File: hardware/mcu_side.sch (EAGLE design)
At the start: 31 parts, among them CON1 JST-ZR-06, Q1 BSS138LT3G, U1 STM32F031G6U6

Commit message: Add start module
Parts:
- added SM_3.3V, SM_GND, SM_KILL, SM_START: PAD-SMD-ROUND-1.27PAD, Isaks Bibliotek:PAD-SMD-ROUND-1.27PAD
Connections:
- new net KILL: SM_KILL.1, U1.PA3
- new net START: SM_START.1, U1.PA2
- net 3.3V: now also SM_3.3V.1
- net GND: now also SM_GND.1
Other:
- note added: "Check before production: - Check Hardware app note - 3.3V reg again. - That the FB on servo indeed is a pot and does not need V_divider - Double check pinout - Double check ERC + DRC - Check Silcscreen"
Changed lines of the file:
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@@
 <drawing>
 <settings>
-<setting alwaysvectorfont="no"/>
+<setting alwaysvectorfont="yes"/>
 <setting verticaltext="up"/>
 </settings>
@@
 <schematic_group name="I2C_PULLUP"/>
 <schematic_group name="STEERING_SERVO_FEEDBACK"/>
+<schematic_group name="START_MODULE"/>
 </groups>
 <parts>
@@
 <part name="SUPPLY13" library="Isaks Bibliotek" library_urn="urn:adsk.eagle:library:11889733" deviceset="3.3V" device=""/>
 <part name="GND14" library="Isaks Bibliotek" library_urn="urn:adsk.eagle:library:11889733" deviceset="GND" device=""/>
+<part name="SM_3.3V" library="Isaks Bibliotek" library_urn="urn:adsk.eagle:library:11889733" deviceset="PAD-SMD-ROUND-1.27" device="PAD" package3d_urn="urn:adsk.eagle:package:13270955/1"/>
+<part name="SM_START" library="Isaks Bibliotek" library_urn="urn:adsk.eagle:library:11889733" deviceset="PAD-SMD-ROUND-1.27" device="PAD" package3d_urn="urn:adsk.eagle:package:13270955/1"/>
+<part name="SUPPLY14" library="Isaks Bibliotek" library_urn="urn:adsk.eagle:library:11889733" deviceset="3.3V" device=""/>
+<part name="GND15" library="Isaks Bibliotek" library_urn="urn:adsk.eagle:library:11889733" deviceset="GND" device=""/>
+<part name="SM_KILL" library="Isaks Bibliotek" library_urn="urn:adsk.eagle:library:11889733" deviceset="PAD-SMD-ROUND-1.27" device="PAD" package3d_urn="urn:adsk.eagle:package:13270955/1"/>
+<part name="SM_GND" library="Isaks Bibliotek" library_urn="urn:adsk.eagle:library:11889733" deviceset="PAD-SMD-ROUND-1.27" device="PAD" package3d_urn="urn:adsk.eagle:package:13270955/1"/>
 </parts>
 <sheets>
@@
 <text x="170.18" y="38.1" size="1.778" layer="97" grouprefs="STEERING_SERVO_FEEDBACK">Servo signal is created by a voltage divider,
 the divider is  a potentiometer in the servo gearbox.</text>
-<wire x1="165.1" y1="45.72" x2="231.14" y2="45.72" width="0.1524" layer="97" grouprefs="STEERING_SERVO_FEEDBACK"/>
-<wire x1="231.14" y1="45.72" x2="231.14" y2="33.02" width="0.1524" layer="97" grouprefs="STEERING_SERVO_FEEDBACK"/>
-<wire x1="231.14" y1="33.02" x2="165.1" y2="33.02" width="0.1524" layer="97" grouprefs="STEERING_SERVO_FEEDBACK"/>
+<wire x1="165.1" y1="45.72" x2="236.22" y2="45.72" width="0.1524" layer="97" grouprefs="STEERING_SERVO_FEEDBACK"/>
+<wire x1="236.22" y1="45.72" x2="236.22" y2="33.02" width="0.1524" layer="97" grouprefs="STEERING_SERVO_FEEDBACK"/>
+<wire x1="236.22" y1="33.02" x2="165.1" y2="33.02" width="0.1524" layer="97" grouprefs="STEERING_SERVO_FEEDBACK"/>
 <wire x1="165.1" y1="33.02" x2="165.1" y2="45.72" width="0.1524" layer="97" grouprefs="STEERING_SERVO_FEEDBACK"/>
+<text x="30.48" y="22.86" size="2.54" layer="94">Check before production:
+- Check Hardware app note
+- 3.3V reg again.
+- That the FB on servo indeed is a pot
+  and does not need V_divider
+- Double check pinout
+- Double check ERC + DRC
+- Check Silcscreen</text>
 </plain>
 <instances>
@@
 <instance part="GND14" gate="1" x="195.58" y="53.34" smashed="yes" grouprefs="STEERING_SERVO_FEEDBACK">
 <attribute name="VALUE" x="195.58" y="53.086" size="1.778" layer="96" align="top-center"/>
+</instance>
+<instance part="SM_3.3V" gate="G$1" x="279.4" y="71.12" smashed="yes" grouprefs="START_MODULE">
+<attribute name="NAME" x="280.67" y="72.39" size="1.778" layer="95" font="vector"/>
+</instance>
+<instance part="SM_START" gate="G$1" x="279.4" y="66.04" smashed="yes" grouprefs="START_MODULE">
+<attribute name="NAME" x="280.67" y="67.31" size="1.778" layer="95" font="vector"/>
+</instance>
+<instance part="SUPPLY14" gate="G$1" x="276.86" y="76.2" smashed="yes" grouprefs="START_MODULE">
+<attribute name="VALUE" x="276.86" y="78.994" size="1.778" layer="96" align="bottom-center"/>
+</instance>
+<instance part="GND15" gate="1" x="276.86" y="50.8" smashed="yes" grouprefs="START_MODULE">
+<attribute name="VALUE" x="276.86" y="50.546" size="1.778" layer="96" align="top-center"/>
+</instance>
+<instance part="SM_KILL" gate="G$1" x="279.4" y="60.96" smashed="yes" grouprefs="START_MODULE">
+<attribute name="NAME" x="280.67" y="62.23" size="1.778" layer="95" font="vector"/>
+</instance>
+<instance part="SM_GND" gate="G$1" x="279.4" y="55.88" smashed="yes" grouprefs="START_MODULE">
+<attribute name="NAME" x="280.67" y="57.15" size="1.778" layer="95" font="vector"/>
 </instance>
 </instances>
@@
 <wire x1="195.58" y1="63.5" x2="195.58" y2="55.88" width="0.1524" layer="91" grouprefs="STEERING_SERVO_FEEDBACK"/>
 </segment>
+<segment>
+<pinref part="SM_GND" gate="G$1" pin="1"/>
+<pinref part="GND15" gate="1" pin="GND"/>
+<wire x1="279.4" y1="55.88" x2="276.86" y2="55.88" width="0.1524" layer="91" grouprefs="START_MODULE"/>
+<wire x1="276.86" y1="55.88" x2="276.86" y2="53.34" width="0.1524" layer="91" grouprefs="START_MODULE"/>
+</segment>
 </net>
 <net name="N$1" class="0">
@@
 <wire x1="195.58" y1="73.66" x2="195.58" y2="78.74" width="0.1524" layer="91" grouprefs="STEERING_SERVO_FEEDBACK"/>
 </segment>
+<segment>
+<pinref part="SM_3.3V" gate="G$1" pin="1"/>
+<pinref part="SUPPLY14" gate="G$1" pin="3.3V"/>
+<wire x1="279.4" y1="71.12" x2="276.86" y2="71.12" width="0.1524" layer="91" grouprefs="START_MODULE"/>
+<wire x1="276.86" y1="71.12" x2="276.86" y2="76.2" width="0.1524" layer="91" grouprefs="START_MODULE"/>
+</segment>
 </net>
 <net name="SDA" class="0">
@@
 </segment>
 </net>
+<net name="KILL" class="0">
+<segment>
+<pinref part="SM_KILL" gate="G$1" pin="1"/>
+<wire x1="279.4" y1="60.96" x2="264.16" y2="60.96" width="0.1524" layer="91" grouprefs="START_MODULE"/>
+<label x="266.7" y="60.96" size="1.778" layer="95" grouprefs="START_MODULE"/>
+</segment>
+<segment>
+<pinref part="U1" gate="G$1" pin="PA3"/>
+<wire x1="121.92" y1="213.36" x2="101.6" y2="213.36" width="0.1524" layer="91"/>
+<label x="104.14" y="213.36" size="1.778" layer="95"/>
+</segment>
+</net>
+<net name="START" class="0">
+<segment>
+<pinref part="SM_START" gate="G$1" pin="1"/>
+<wire x1="279.4" y1="66.04" x2="264.16" y2="66.04" width="0.1524" layer="91" grouprefs="START_MODULE"/>
+<label x="266.7" y="66.04" size="1.778" layer="95" grouprefs="START_MODULE"/>
+</segment>
+<segment>
+<pinref part="U1" gate="G$1" pin="PA2"/>
+<wire x1="121.92" y1="215.9" x2="101.6" y2="215.9" width="0.1524" layer="91"/>
+<label x="104.14" y="215.9" size="1.778" layer="95"/>
+</segment>
+</net>

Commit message: Added todo before production
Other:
- note added: "TODO: - Add encoder input for drive motor. Check before production: - Check Hardware app note for stm32 f0 - 3.3V regulator values - That the FB on servo indeed is a pot and does not need V_divider - Double check pinout - Double check ERC + DRC - Check Silcscreen"
- note removed: "Check before production: - Check Hardware app note - 3.3V reg again. - That the FB on servo indeed is a pot and does not need V_divider - Double check pinout - Double check ERC + DRC - Check Silcscreen"
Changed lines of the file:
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@@
 <wire x1="236.22" y1="33.02" x2="165.1" y2="33.02" width="0.1524" layer="97" grouprefs="STEERING_SERVO_FEEDBACK"/>
 <wire x1="165.1" y1="33.02" x2="165.1" y2="45.72" width="0.1524" layer="97" grouprefs="STEERING_SERVO_FEEDBACK"/>
-<text x="30.48" y="22.86" size="2.54" layer="94">Check before production:
-- Check Hardware app note
-- 3.3V reg again.
+<text x="30.48" y="12.7" size="2.54" layer="94">TODO:
+- Add encoder input for drive motor.
+Check before production:
+- Check Hardware app note for stm32 f0
+- 3.3V regulator values
 - That the FB on servo indeed is a pot
   and does not need V_divider

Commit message: Production ready
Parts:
- added ENC_3.3V, ENC_A, ENC_B, ENC_GND: PAD-SMD-ROUND-1.27PAD, Isaks Bibliotek:PAD-SMD-ROUND-1.27PAD
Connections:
- new net ENC_A: ENC_A.1, U1.PB4
- new net ENC_B: ENC_B.1, U1.PB5
- net 3.3V: now also ENC_3.3V.1
- net GND: now also ENC_GND.1
- net MOTOR_DIR: now also U1.PB6; no longer U1.PB5
- net STEER_DIR: now also U1.PB7; no longer U1.PB4
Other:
- note added: "Check before production: - That the FB on servo indeed is a pot and does not need V_divider"
- note removed: "TODO: - Add encoder input for drive motor. Check before production: - Check Hardware app note for stm32 f0 - 3.3V regulator values - That the FB on servo indeed is a pot and does not need V_divider - Double check pinout - Double check ERC + DRC - Check Silcscreen"
- moved on the sheet: SM_3.3V, SM_GND, SM_KILL, SM_START

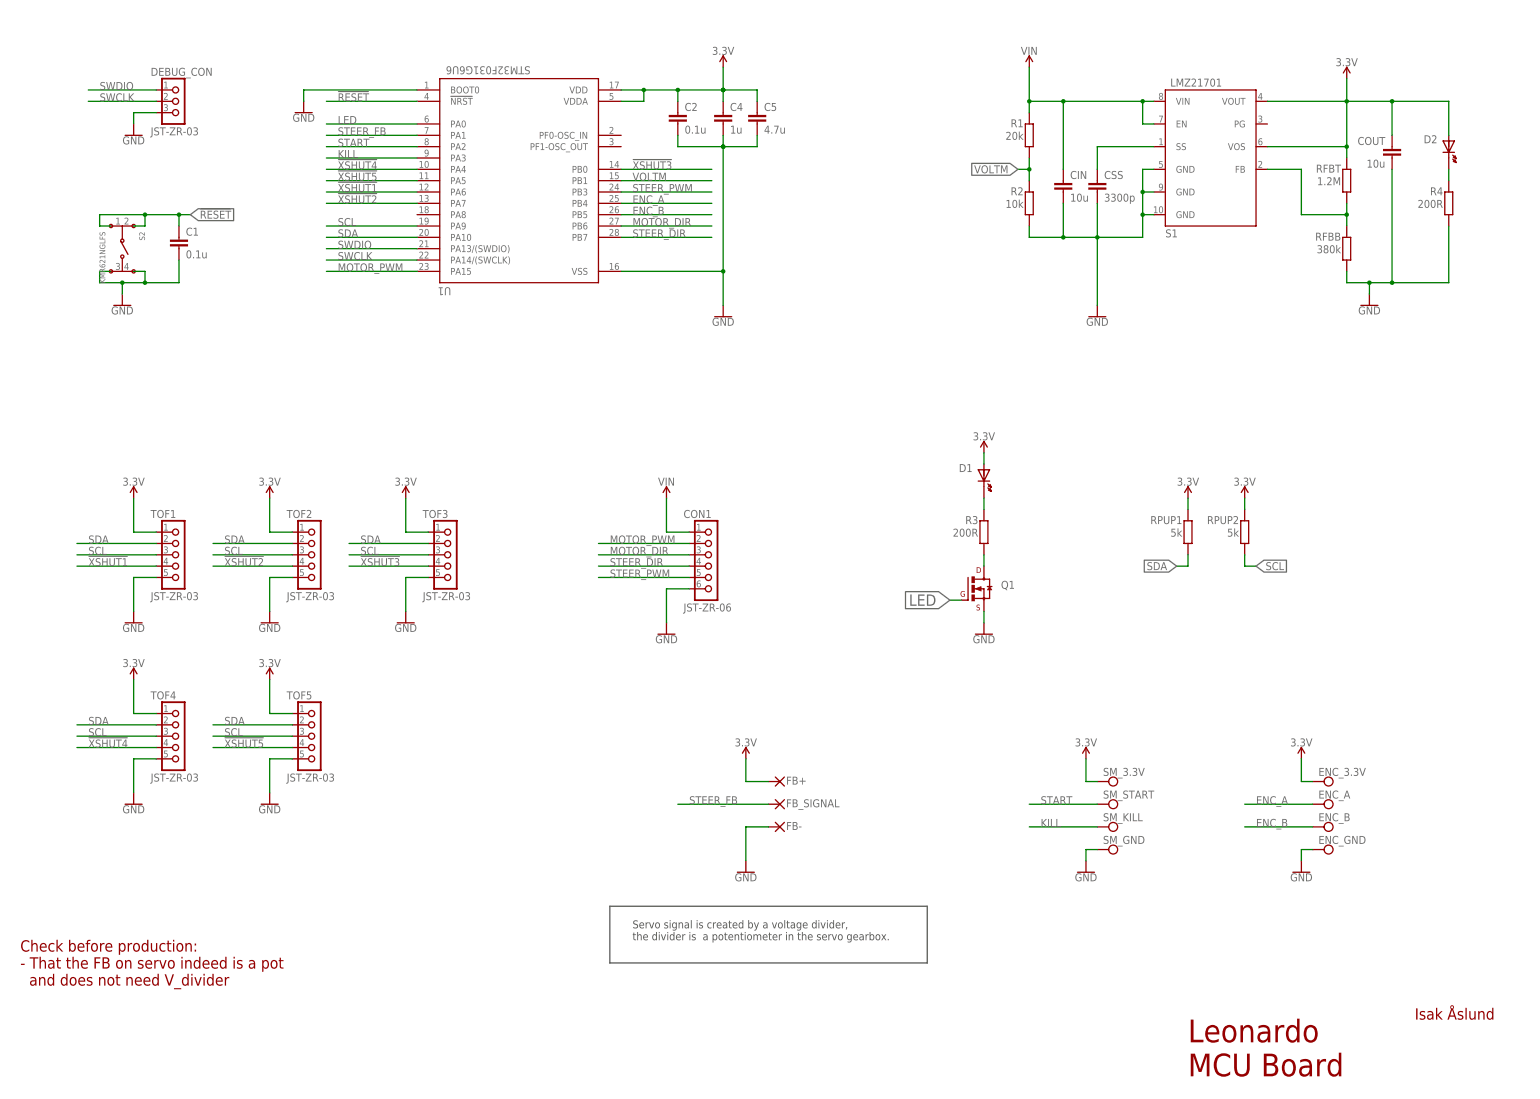
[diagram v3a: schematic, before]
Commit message: VReg changed to linear LM1117, 3.3V
The switching VREG burned the MCU twice..... Switched to an old classic :)
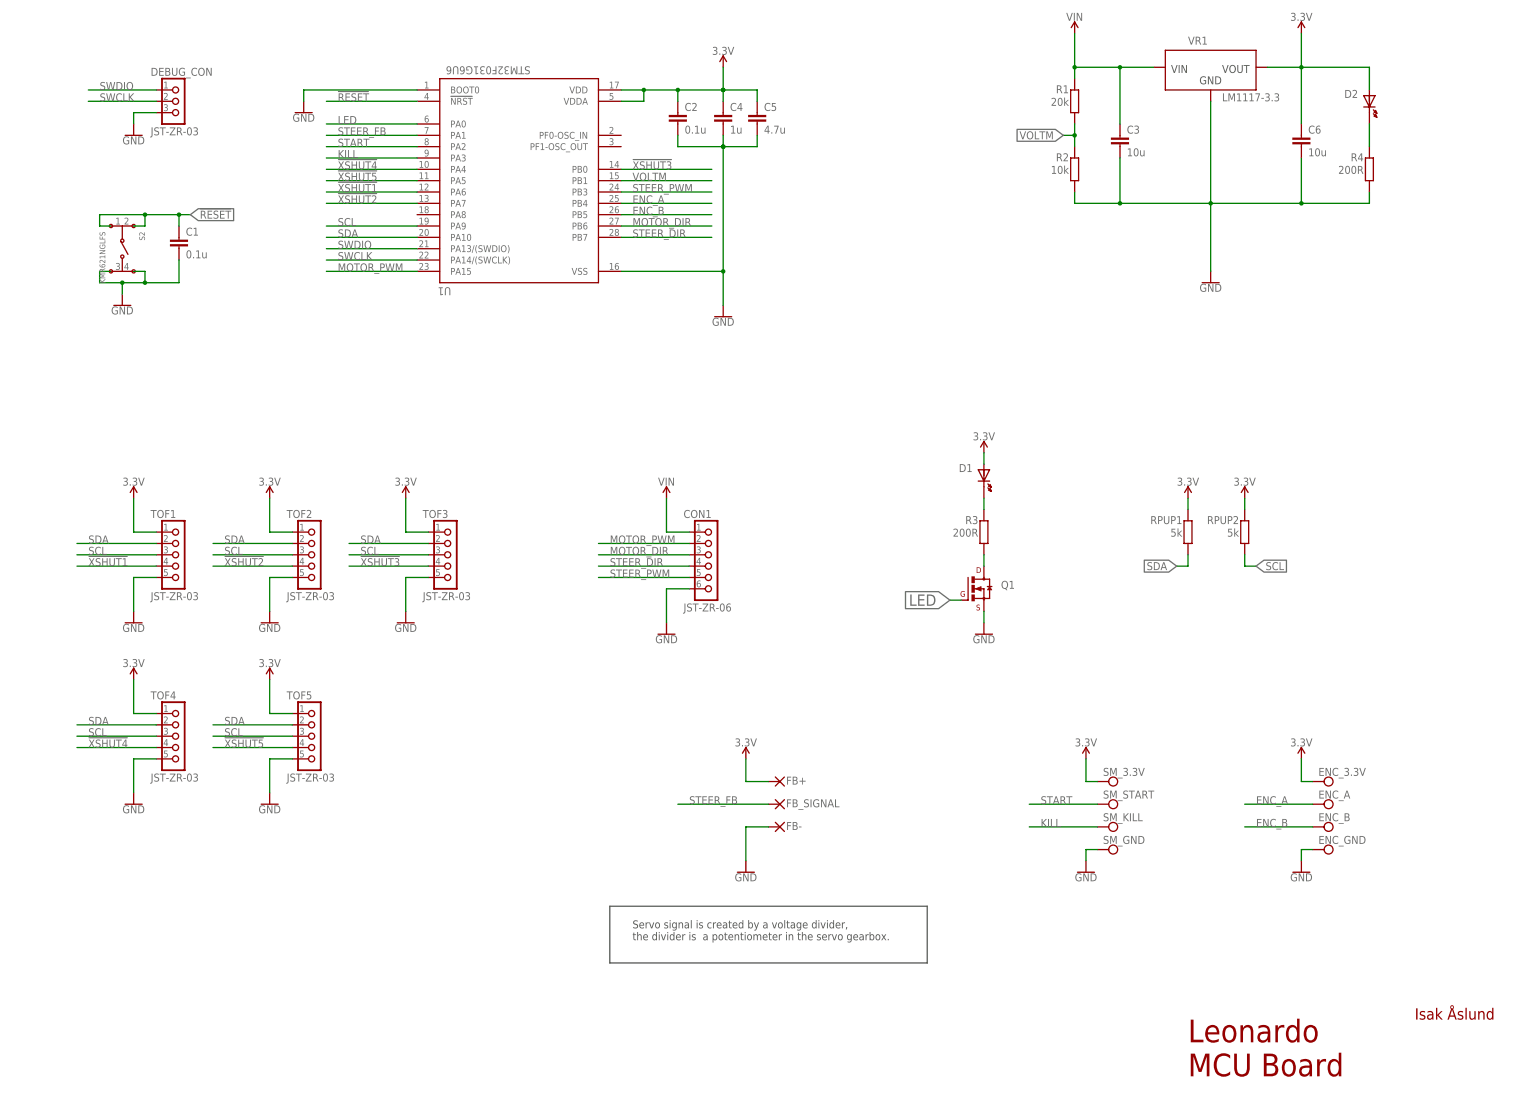
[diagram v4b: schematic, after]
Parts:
- removed CIN, COUT: 10u, CASE-RCL:C0805
- removed CSS: 3300p, CASE-RCL:C0603
- removed RFBB: 380k, CASE-RCL:R0603
- removed RFBT: 1.2M, CASE-RCL:R0603
- removed S1: LMZ21701, Isaks Bibliotek:LMZ21701
- added C3, C6: 10u, CASE-RCL:C1206
- added VR1: LM1117-3.3, Isaks Bibliotek:LM1117-3.3
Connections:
- removed net N$1: CSS.1, S1.SS
- removed net N$3: RFBB.1, RFBT.1, S1.FB
- net 3.3V: now also C6.1, VR1.VOUT; no longer COUT.1, RFBT.2, S1.VOS, S1.VOUT
- net GND: now also C3.2, C6.2, VR1.GND; no longer CIN.2, COUT.2, CSS.2, RFBB.2, S1.GND@1, S1.GND@2, S1.GND@3
- net VIN: now also C3.1, VR1.VIN; no longer CIN.1, S1.EN, S1.VIN
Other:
- note removed: "Check before production: - That the FB on servo indeed is a pot and does not need V_divider"
- moved on the sheet: D2, R1, R2, R4
